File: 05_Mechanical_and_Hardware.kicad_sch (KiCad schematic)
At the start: 14 parts

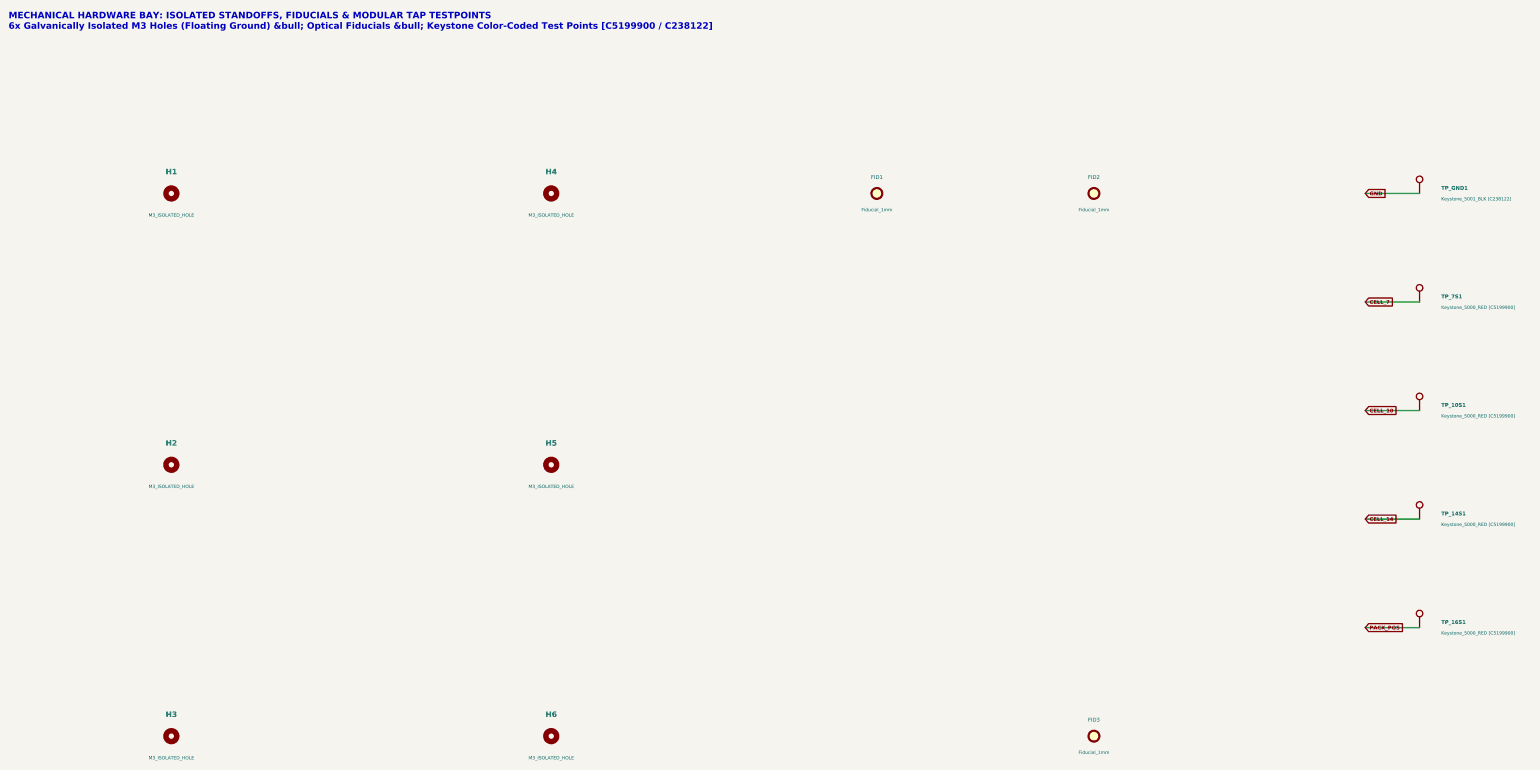
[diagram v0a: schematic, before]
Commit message: Convert pack to 14S with 7 NTC sensors, JST XH harness connectors, all-JLC BOM
- Schematic regenerated: 14 cells, 15-wire BMS sense on JST XH B15B-XH-A,
  7x 10k B3950 NTC saddles on JST XH B14B-XH-A, per-cell test loops and
  reverse-insertion indicator, power path with 5x20 fuse and M4 lugs.
- Fixes: HV zener was reversed, 4.7k/1206 HV LED resistor dissipated 0.68W
  (now 22k), 24V PPTCs on sense taps replaced with 60V MF-MSMF010-2,
  fuse-blown LED polarity corrected.
- Banana jacks (not stocked at LCSC) replaced by Keystone 5000/5001 loops.
- PCB re-laid out on the A4 (297x210) 4-layer outline: 8+6 cell columns,
  zones for cell links, sense routed on In1, NTC pairs on In2.
- ERC 0, DRC 0 (all severities), 0 unconnected, 0 schematic parity issues.
- Added Gerbers/drill zip, JLCPCB BOM + CPL, schematic PDF, renders, and the
  generator scripts in tools/.

Co-Authored-By: Claude Opus 5.5 <noreply@anthropic.com>
Claude-Session: https://claude.ai/code/session_01SDBUxKR8a94h5ECbt5NLbF
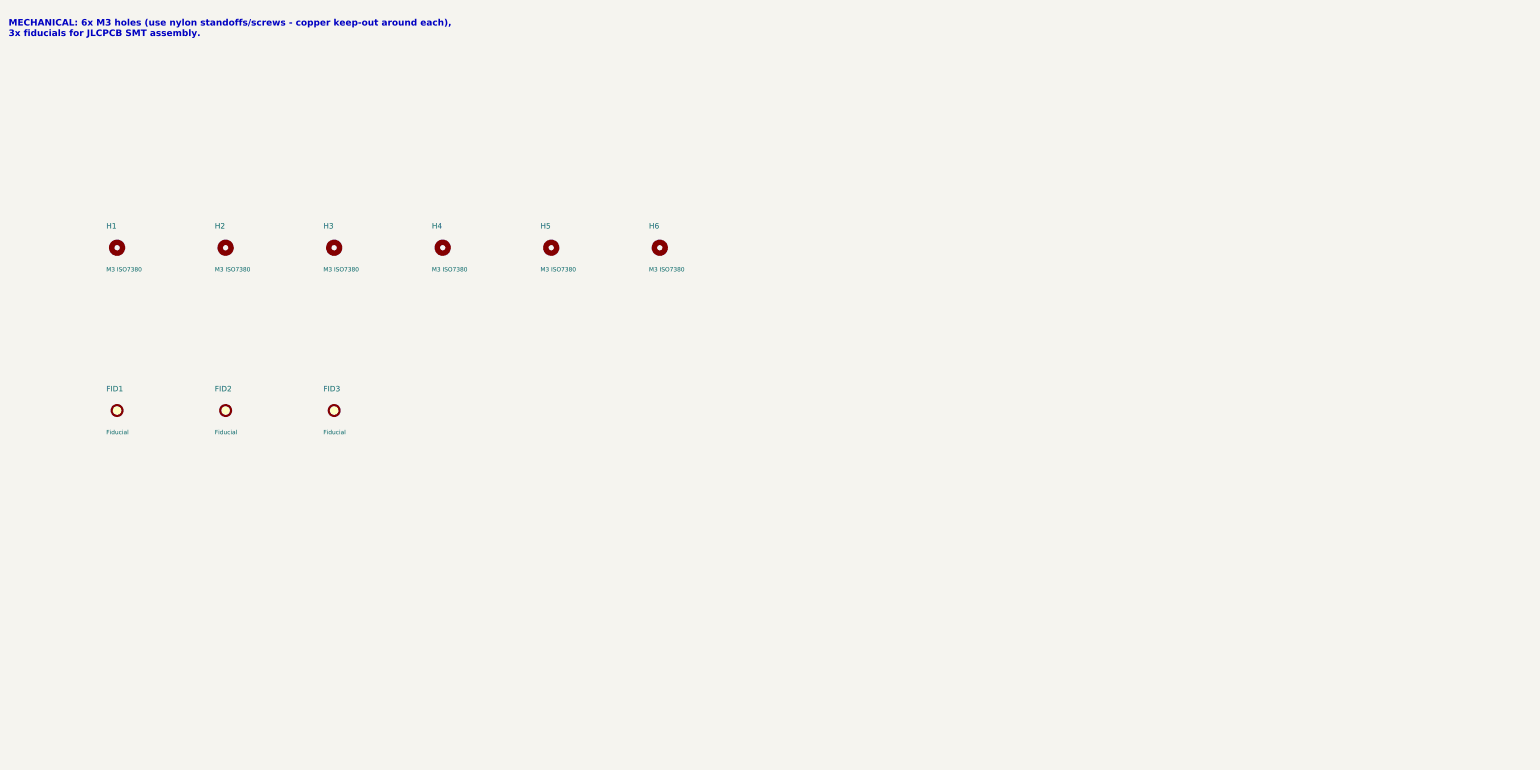
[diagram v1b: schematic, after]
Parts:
- removed TP_10S1, TP_14S1, TP_16S1, TP_7S1: Keystone_5000_RED [C5199900], TestPoint:TestPoint_Keystone_5000-5004_Miniature, symbol Connector:TestPoint
- removed TP_GND1: Keystone_5001_BLK [C238122], TestPoint:TestPoint_Keystone_5000-5004_Miniature, symbol Connector:TestPoint
- FID1, FID2, FID3: value Fiducial_1mm -> Fiducial; now left out of the parts list
- H1, H2, H3, H4, H5, H6: value M3_ISOLATED_HOLE -> M3 ISO7380; now left out of the parts list
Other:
- note added: "MECHANICAL: 6x M3 holes (use nylon standoffs/screws - copper keep-out around each), 3x fiducials for JLCPCB SMT assembly."
- note removed: "MECHANICAL HARDWARE BAY: ISOLATED STANDOFFS, FIDUCIALS & MODULAR TAP TESTPOINTS 6x Galvanically Isolated M3 Holes (Floating Ground) &bull; Optical Fiducials &bull; Keystone Color-Coded Test Points [C5199900 / C238122]"
- company: Antigravity Battery Engineering -> Battery Pack Breakout - 14S / A4
- title: MECHANICAL HARDWARE: ISOLATED STANDOFFS, TEST POINTS & FIDUCIALS -> MECHANICAL: MOUNTING HOLES & FIDUCIALS

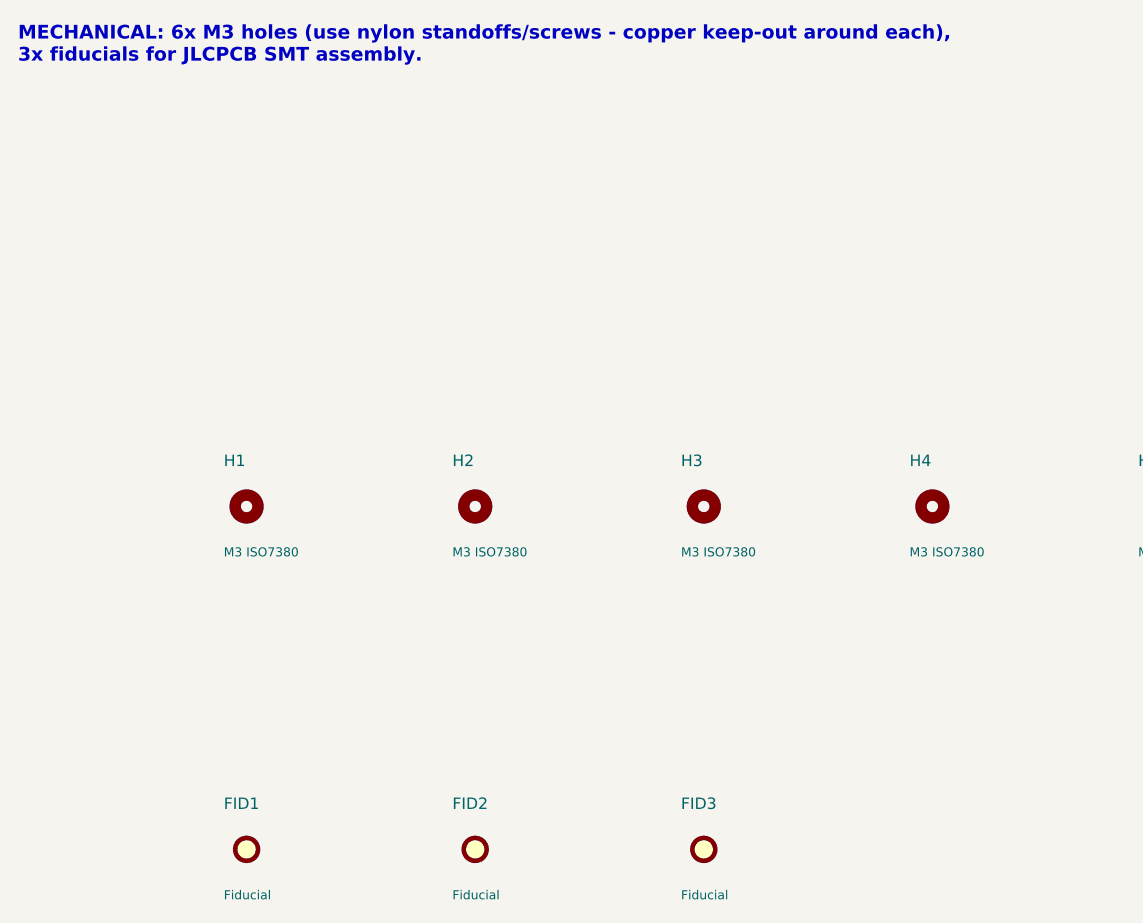
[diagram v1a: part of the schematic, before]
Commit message: Make the board mirror-symmetric about its centre line
- NTCs: 3 per side in mirrored gaps, NTC4 on the centre line at the
  cell 7->8 bus (J2 pins 7/8); J2 pin 2n-1/2n = NTCn kept.
- Sense spine exactly symmetric: tap-7 PPTC and its bus line on the centre
  line, side buses mirrored, J1 fan symmetric.
- Per-cell LED strings: series order chosen per cell so mirrored twins use
  the same parts in the same places (function unchanged).
- TVS chain under J1 mirrored; the centre pair stands vertically either side
  of lane 7.
- HV indicator + pack TVS centred at J2's mirror position; top-band copper
  mirrored; 4 corner fiducials.
- tools/symcheck.py audits mirror partners: only J2, the HV block and the
  single PACK+ fuse (+ its LED) are one-of-a-kind.
- ERC 0, DRC 0, 0 unconnected, 0 parity; ACIR spread 0.08 %.

Co-Authored-By: Claude Opus 5.5 <noreply@anthropic.com>
Claude-Session: https://claude.ai/code/session_01SDBUxKR8a94h5ECbt5NLbF
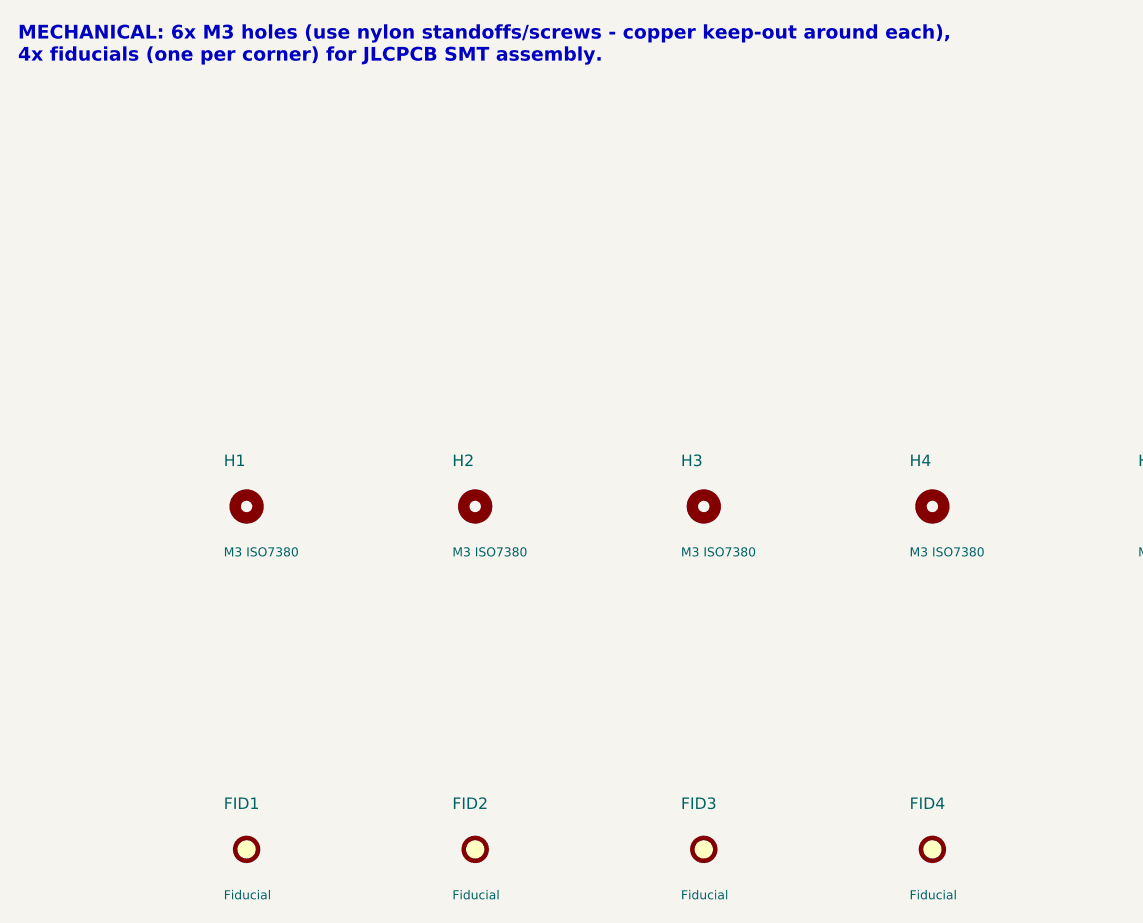
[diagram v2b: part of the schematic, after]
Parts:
- added FID4: Fiducial, Fiducial:Fiducial_1mm_Mask2mm, symbol Mechanical:Fiducial
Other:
- note added: "MECHANICAL: 6x M3 holes (use nylon standoffs/screws - copper keep-out around each), 4x fiducials (one per corner) for JLCPCB SMT assembly."
- note removed: "MECHANICAL: 6x M3 holes (use nylon standoffs/screws - copper keep-out around each), 3x fiducials for JLCPCB SMT assembly."
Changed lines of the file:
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@@
 		(comment 2 "All parts JLCPCB/LCSC sourced - LCSC field on every symbol")
 	)
-	(text "MECHANICAL: 6x M3 holes (use nylon standoffs/screws - copper keep-out around each),\n3x fiducials for JLCPCB SMT assembly."
+	(text "MECHANICAL: 6x M3 holes (use nylon standoffs/screws - copper keep-out around each),\n4x fiducials (one per corner) for JLCPCB SMT assembly."
 		(exclude_from_sim no)
 		(at 25.4 22.86 0)
@@
 					(unit 1)
 				)
+			)
+		)
+	)
+	(symbol
+		(lib_id "Mechanical:Fiducial")
+		(at 127 114.3 0)
+		(unit 1)
+		(body_style 1)
+		(exclude_from_sim no)
+		(in_bom no)
+		(on_board yes)
+		(in_pos_files yes)
+		(dnp no)
+		(property "Reference" "FID4"
+			(at 124.46 109.22 0)
+			(show_name no)
+			(do_not_autoplace no)
+			(effects
+				(font
+					(size 1.27 1.27)
+				)
+				(justify left)
+			)
+		)
+		(property "Value" "Fiducial"
+			(at 124.46 119.38 0)
+			(show_name no)
+			(do_not_autoplace no)
+			(effects
+				(font
+					(size 1 1)
+				)
+				(justify left)
+			)
+		)
+		(property "Footprint" "Fiducial:Fiducial_1mm_Mask2mm"
+			(at 127 114.3 0)
+			(hide yes)
+			(show_name no)
+			(do_not_autoplace no)
+			(effects
+				(font
+					(size 1.27 1.27)
+				)
+			)
+		)
+		(property "Datasheet" ""
+			(at 127 114.3 0)
+			(hide yes)
+			(show_name no)
+			(do_not_autoplace no)
+			(effects
+				(font
+					(size 1.27 1.27)
+				)
+			)
+		)
+		(property "Description" "Assembly fiducial"
+			(at 127 114.3 0)
+			(hide yes)
+			(show_name no)
+			(do_not_autoplace no)
+			(effects
+				(font
+					(size 1.27 1.27)
+				)
+			)
+		)
+		(instances
+			(project "BatteryPack_16S_A4_Breakout"
+				(path "/00000000-0000-0000-0000-000000000001/00000000-0000-0000-0000-000000000006"
+					(reference "FID4")
+					(unit 1)
+				)
